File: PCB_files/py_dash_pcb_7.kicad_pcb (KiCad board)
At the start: 4 copper layers, 203.8 x 102.4 mm, 104 parts, among them J1 FFC2B28-40-G, J2 CANbus, J3 uUSB, Q1 DMG2307, Q2 DMG2307, Q3 DMG2307, SW1 SW_Push, SW2 SW_Push, SW3 SW_Push, SW4 SW_Push, SW5 SW_Push, SW6 SW_Push, SW7 nBoot, U1 CM4102008, U2 FSUSB42MUX, U3 AP64501SP-13, U4 TPD8S009DSMR, U5 TPD8S009DSMR, U6 TPD2EUSB30, U7 SN65HVD234, U8 MCP2515-xST, U9 BD33FC0FP, Y1 16Mhz

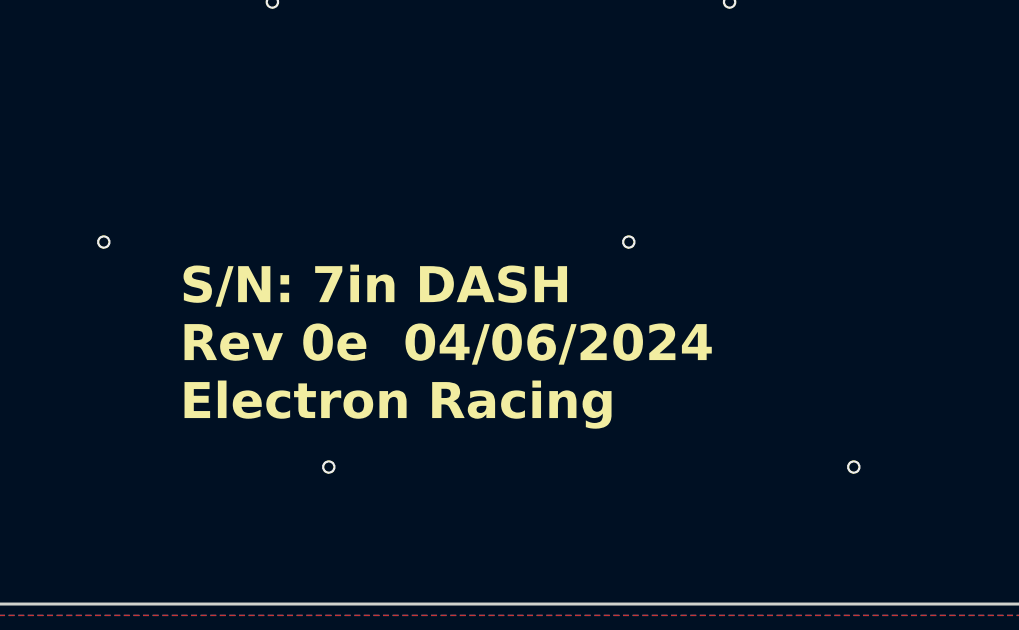
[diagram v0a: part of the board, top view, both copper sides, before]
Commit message: r1a upload
uploaded files for r1a; correct button numbering
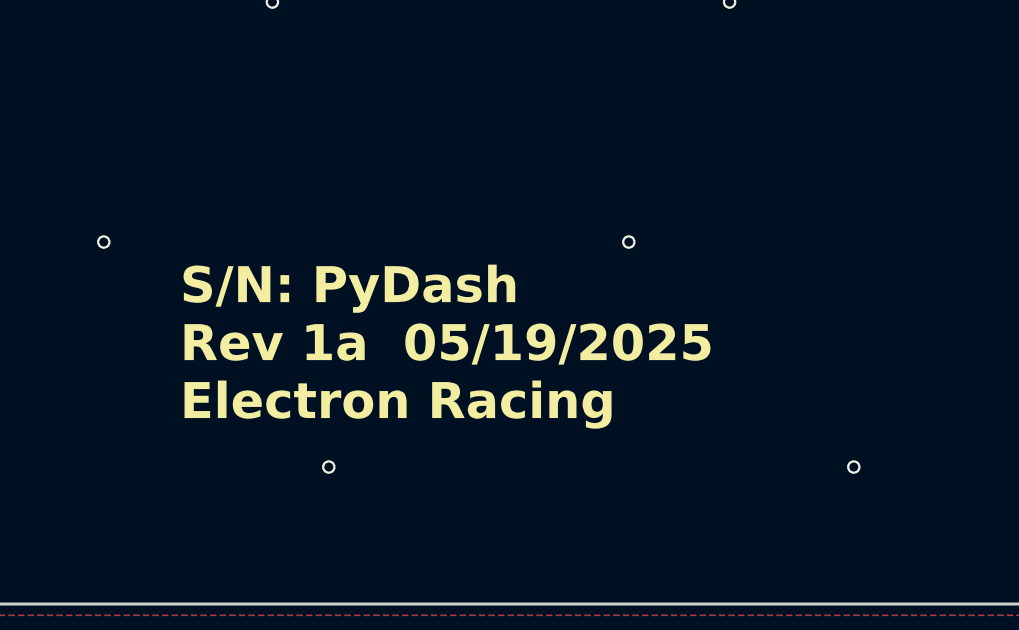
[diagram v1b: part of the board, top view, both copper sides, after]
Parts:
- R28, R29: value 2k2 -> 2k2 1%
- renumbered SW4 to SW1, SW5 to SW2, SW6 to SW3, SW1 to SW4, SW2 to SW5, SW3 to SW6
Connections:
- C26 pad 1: btn_L1 -> btn_R1
- C27 pad 1: btn_L2 -> btn_R2
- C28 pad 1: btn_L3 -> btn_R3
- C29 pad 1: btn_R1 -> btn_L1
- C30 pad 1: btn_R2 -> btn_L2
- C31 pad 1: btn_R3 -> btn_L3
- R15 pad 1: btn_L1 -> btn_R1
- R16 pad 1: btn_L2 -> btn_R2
- R17 pad 1: btn_L3 -> btn_R3
- R21 pad 1: btn_R1 -> btn_L1
- R22 pad 1: btn_R2 -> btn_L2
- R23 pad 1: btn_R3 -> btn_L3
- U1 pad 26: btn_R2 -> btn_L2
- U1 pad 30: btn_R3 -> btn_L3
- U1 pad 45: btn_R1 -> btn_L1
- U1 pad 48: btn_L3 -> btn_R3
- U1 pad 54: btn_L2 -> btn_R2
- U1 pad 58: btn_L1 -> btn_R1
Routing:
- net btn_R1: track 118.1 -> 95.6 mm, vias 0 -> 2
- net btn_L1: track 95.6 -> 118.1 mm, vias 2 -> 0
- net btn_R3: track 154.1 -> 138.1 mm
- net btn_L3: track 138.1 -> 154.1 mm
- net btn_R2: track 129.0 -> 114.8 mm
- net btn_L2: track 114.8 -> 129.0 mm
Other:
- board text added: "S/N: PyDash Rev 1a 05/19/2025 Electron Racing"
- board text removed: "S/N: 7in DASH Rev 0e 04/06/2024 Electron Racing"

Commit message: Rev2a initial upload
PCB files
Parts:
- removed C34: 0u1, Capacitor_SMD:C_0805_2012Metric
- removed J3: uUSB, user:GCT_USB3140-30-0170-1-C_REVE1
- removed R28, R29: 2k2 1%, Resistor_SMD:R_0805_2012Metric
- removed U2: FSUSB42MUX, Package_SO:MSOP-10_3x3mm_P0.5mm
- added C21: 0u1, Capacitor_SMD:C_0805_2012Metric, F.Cu at (215.2, 57.8)
- added C35: 10u, Capacitor_SMD:C_0805_2012Metric, F.Cu at (213.1, 57.8)
- added J5: Micro_SD_Card_Det1, Connector_Card:microSD_HC_Hirose_DM3AT-SF-PEJM5, F.Cu at (224.3, 53.6)
- added J8: USB_C_Receptacle_USB2.0_14P, Connector_USB:USB_C_Receptacle_GCT_USB4115-03-C, F.Cu at (198.2, 118.5)
- added U10: EMIF06-MSD02N16, user:EMIF06MSD02N16, F.Cu at (209.7, 60.9)
- moved U6 97.7 mm to (192.0, 115.9)
- moved C33 7.42 mm to (139.7, 48.4), turned to 180 degrees
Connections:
- J1 pad 7: tch_USBD- -> unconnected-(J1-Pad7)
- J1 pad 8: tch_USBD+ -> unconnected-(J1-Pad8)
- U1 pad 101: USB_OTG -> GND
- U1 pad 103: USBD- -> ext_USBD-
- U1 pad 105: USBD+ -> ext_USBD+
- U1 pad 24: unconnected-(U1A-GPIO26-Pad24) -> SD_DET
- U1 pad 57: unconnected-(U1A-SD_CLK-Pad57) -> SD_CLK
- U1 pad 61: unconnected-(U1A-SD_DAT3-Pad61) -> SD_DAT3
- U1 pad 62: unconnected-(U1A-SD_CMD-Pad62) -> SD_CMD
- U1 pad 63: unconnected-(U1A-SD_DAT0-Pad63) -> SD_DAT0
- U1 pad 67: unconnected-(U1A-SD_DAT1-Pad67) -> SD_DAT1
- U1 pad 69: unconnected-(U1A-SD_DAT2-Pad69) -> SD_DAT2
- U5 pad 4: tch_USBD- -> unconnected-(U5-D1+-Pad4)
- U5 pad 6: tch_USBD+ -> unconnected-(U5-D1--Pad6)
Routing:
- net SD_DET: track 0.00 -> 86.4 mm, vias 0 -> 2
- net SD_DAT2: track 0.00 -> 82.0 mm
- net SD_DAT1: track 0.00 -> 77.0 mm
- net SD_DAT0: track 0.00 -> 75.1 mm, vias 0 -> 2
- net SD_DAT3: track 0.00 -> 74.5 mm, vias 0 -> 2
- net SD_CLK: track 0.00 -> 70.8 mm, vias 0 -> 2
- net USB_OTG: track 68.6 -> 0.00 mm, vias 2 -> 0
- net SD_CMD: track 0.00 -> 68.1 mm, vias 0 -> 2
- net USBD-: track 57.7 -> 0.00 mm
- net USBD+: track 56.9 -> 0.00 mm
- net +3.3V: track 302.8 -> 350.5 mm, vias 22 -> 24
- net ext_USBD+: track 19.1 -> 58.3 mm, vias 0 -> 5
- net ext_USBD-: track 18.3 -> 55.3 mm, vias 0 -> 2
- net Net-(J5-DAT1): track 0.00 -> 31.3 mm
- net tch_USBD+: track 31.1 -> 0.00 mm
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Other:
- board text added: "S/N: PyDash Rev 2a 02/15/2025 LRC"
- board text added: "uSD"
- board text removed: "S/N: PyDash Rev 1a 05/19/2025 Electron Racing"

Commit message: push from desktop to align files
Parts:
- removed H7: MountingHole, MountingHole:MountingHole_3.2mm_M3_DIN965_Pad
- added H1: MountingHole_M2, MountingHole:MountingHole_3.2mm_M3_DIN965_Pad_TopOnly, F.Cu at (60.2, 57.4)
- added H10: Standoff_M2.5_5ET, user:Standoff_M2.5_5ET, F.Cu at (56.6, 108.7)
- added H11: Standoff_M2.5_5ET, user:Standoff_M2.5_5ET, F.Cu at (56.6, 141.6)
- added H12: Standoff_M2.5_5ET, user:Standoff_M2.5_5ET, F.Cu at (249.4, 50.2)
- added H13: Standoff_M2.5_5ET, user:Standoff_M2.5_5ET, F.Cu at (249.5, 83.1)
- added H14: Standoff_M2.5_5ET, user:Standoff_M2.5_5ET, F.Cu at (249.4, 108.6)
- added H15: Standoff_M2.5_5ET, user:Standoff_M2.5_5ET, F.Cu at (249.4, 141.6)
- added H16: Standoff_M2.5_5ET, user:Standoff_M2.5_5ET, F.Cu at (104.8, 50.1)
- added H17: Standoff_M2.5_5ET, user:Standoff_M2.5_5ET, F.Cu at (104.8, 141.5)
- added H18: Standoff_M2.5_5ET, user:Standoff_M2.5_5ET, F.Cu at (153.0, 50.2)
- added H19: Standoff_M2.5_5ET, user:Standoff_M2.5_5ET, F.Cu at (153.0, 141.3)
- added H20: Standoff_M2.5_5ET, user:Standoff_M2.5_5ET, F.Cu at (201.2, 50.2)
- added H21: Standoff_M2.5_5ET, user:Standoff_M2.5_5ET, F.Cu at (201.2, 141.3)
- added H22: Standoff_M2.5_5ET, user:Standoff_M2.5_5ET, F.Cu at (104.9, 95.8)
- added H23: Standoff_M2.5_5ET, user:Standoff_M2.5_5ET, F.Cu at (201.2, 95.8)
- added H3: MountingHole_M2, MountingHole:MountingHole_3.2mm_M3_DIN965_Pad_TopOnly, F.Cu at (60.2, 134.4)
- added H9: Standoff_M2.5_5ET, user:Standoff_M2.5_5ET, F.Cu at (56.6, 83.1)
- H5, H6: value MountingHole -> MountingHole_M2; footprint MountingHole:MountingHole_3.2mm_M3_DIN965_Pad -> MountingHole:MountingHole_3.2mm_M3_DIN965_Pad_TopOnly
- H8: value MountingHole -> Standoff_M2.5_5ET; footprint MountingHole:MountingHole_3.2mm_M3_DIN965_Pad -> user:Standoff_M2.5_5ET
- moved H5 207.0 mm to (245.8, 134.4)
- moved H8 91.3 mm to (56.6, 50.2)
- moved TP4 42.6 mm to (83.7, 138.8)
- moved J3 9.65 mm to (207.8, 119.7)
- moved U7 9.65 mm to (201.6, 117.1)
- moved H6 7.77 mm to (245.9, 57.3)
- moved C23 7.11 mm to (210.1, 52.8)
- moved C24 7.11 mm to (207.9, 52.8)
- moved SW1 6.42 mm to (116.3, 63.2), turned to 180 degrees
- moved J1 4.64 mm to (219.7, 53.3)
- moved D6 3.92 mm to (124.6, 138.9)
- moved R10 3.92 mm to (128.3, 138.9)
- moved TP3 3.92 mm to (131.7, 138.9)
- moved U4 3.92 mm to (206.6, 58.5), turned to -90 degrees
- moved D3 3.86 mm to (114.6, 131.6)
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- renumbered C33 to C1, C7 to C10, C9 to C11, C14 to C13, C16 to C14, C17 to C15, C18 to C16, C19 to C17, C20 to C18, C4 to C19, C32 to C2, C10 to C20, C3 to C21, C8 to C22, C21 to C23, C35 to C24, C22 to C25, C29 to C27, C27 to C28, C30 to C29, C11 to C3, C28 to C30, C23 to C32, C24 to C33, C25 to C34, C13 to C4, C1 to C5, C2 to C6, C15 to C7, C5 to C8, C6 to C9, D10 to D1, D7 to D2, D4 to D3, D5 to D4, D6 to D5, D1 to D6, D2 to D7, D3 to D8, D8 to D9, J5 to J1, J1 to J2, J8 to J3, J2 to J4, Q3 to Q2, Q2 to Q3, R27 to R1, R2 to R10, R3 to R11, R4 to R12, R18 to R13, R24 to R14, R21 to R16, R19 to R17, R25 to R18, R16 to R19, R9 to R2, R22 to R20, R14 to R21, R20 to R22, R26 to R23, R17 to R24, R23 to R25, R13 to R26, R11 to R3, R6 to R4, R10 to R5, R12 to R6, R5 to R8, R8 to R9, SW7 to SW1, SW4 to SW2, SW1 to SW3, SW5 to SW4, SW2 to SW5, SW3 to SW7, TP4 to TP1, TP1 to TP2, TP2 to TP3, TP3 to TP4, U3 to U2, U9 to U3, U10 to U4, U4 to U5, U5 to U6, U6 to U7, U7 to U9
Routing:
- net +3.3V: track 350.5 -> 364.2 mm, vias 24 -> 22
- net ext_USBD+: track 58.3 -> 68.3 mm
- net ext_USBD-: track 55.3 -> 65.4 mm
- net SD_DET: track 86.4 -> 78.9 mm, vias 2 -> 3
- net Net-(J1-DAT1): track 31.3 -> 24.0 mm
- net Net-(J1-DAT0): track 27.3 -> 21.6 mm
- net SD_DAT2: track 82.0 -> 76.3 mm
- net SD_CMD: track 68.1 -> 62.8 mm
- net Net-(J1-CLK): track 23.3 -> 18.5 mm
- net Net-(J1-CMD): track 19.1 -> 15.2 mm
- net btn_L1: track 120.3 -> 116.8 mm
- net Net-(J1-DAT3/CD): track 16.2 -> 13.3 mm
- net SD_DAT3: track 74.5 -> 72.0 mm, vias 2 -> 0
- net Net-(J1-DAT2): track 13.2 -> 11.5 mm
- net GND: track 4.85 -> 6.40 mm, vias 379 -> 400
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- added copper zone on F.Cu, net Net-(D4-K)
- removed copper zone on F.Cu, net Net-(D3-K)
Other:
- board size 203.8 x 102.4 mm -> 203.8 x 102.3 mm

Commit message: resolved tracker TODOs
Updated USBC placement to work with enclosure. Updated HDMI routes with chosen stackup to meet design requirements. Re-generated PCB fab files.
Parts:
- moved J3 10.9 mm to (218.7, 119.7)
- moved U7 10.9 mm to (212.5, 117.1)
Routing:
- net ext_USBD-: track 65.4 -> 76.3 mm
- net ext_USBD+: track 68.3 -> 79.3 mm
- net CK+: track 69.5 -> 74.6 mm
- net CK-: track 68.8 -> 73.8 mm
- net D0-: track 71.4 -> 75.4 mm
- net D0+: track 72.2 -> 76.1 mm
- net D2-: track 77.2 -> 76.3 mm
- net D2+: track 78.0 -> 77.0 mm
- net D1-: track 74.4 -> 73.8 mm
- net D1+: track 75.1 -> 74.6 mm
- added copper zone on F.Cu, net Net-(D3-K)
- removed copper zone on F.Cu, net Net-(D4-K)
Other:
- board text added: "PyDash - LRC Batch: B/N 03092025 Rev 2a 03/09/2025"
- board text added: "Stackup to be used: JLC04121H-3313 (or equivalent) - 1oz (0.035mm) outer layer - top/bot to inner layer separation 0.1mm Failure to use chosen or equivalent stackup may result in out of spec HDMI routing"
- board text removed: "S/N: PyDash Rev 2a 02/15/2025 LRC"

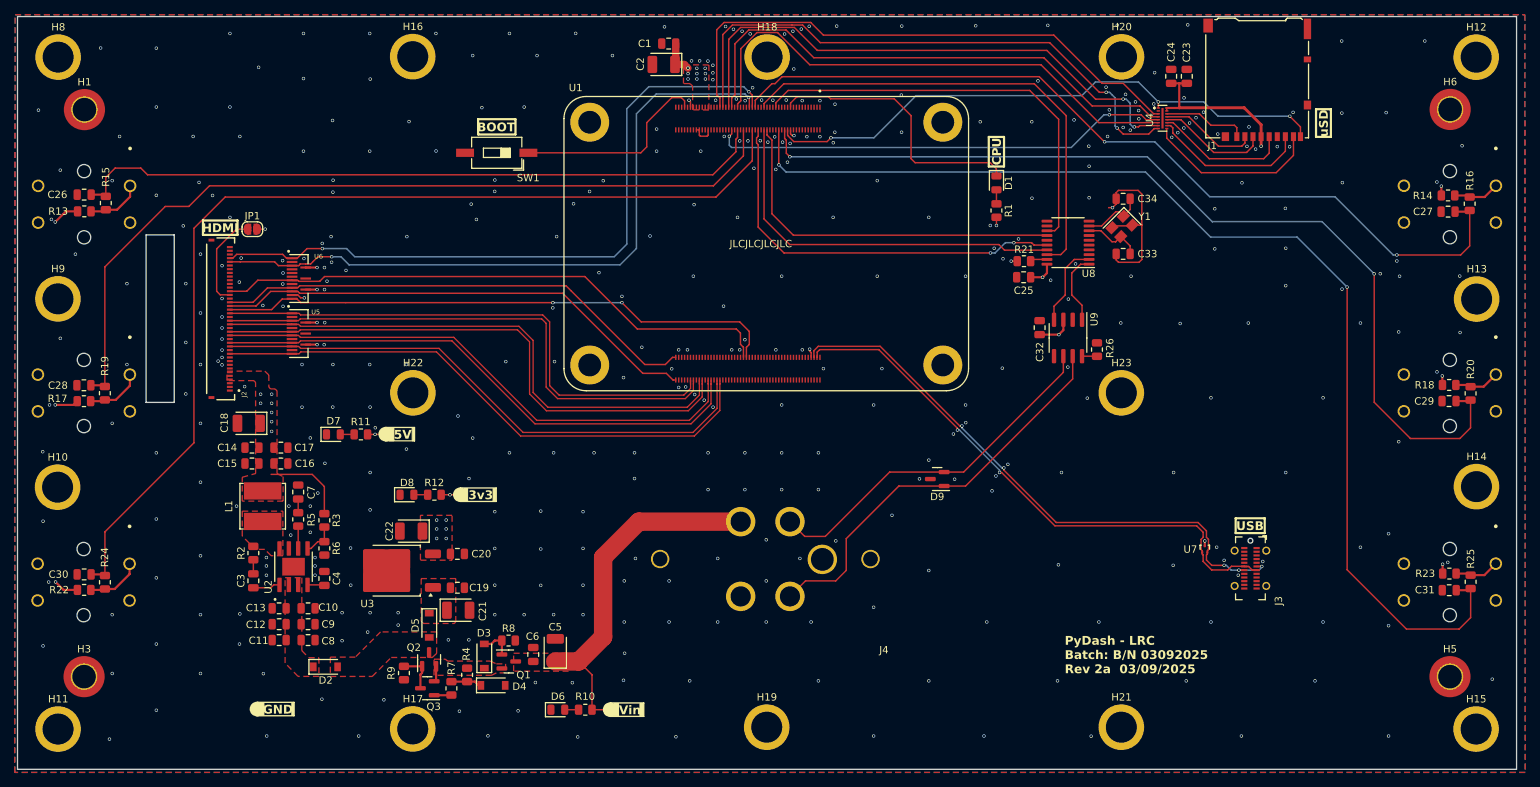
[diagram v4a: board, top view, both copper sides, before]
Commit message: final BOM and tweaking
Tweaked some dimensions after mechanical assembly. Generated BOM and reviewed against reseller inventory
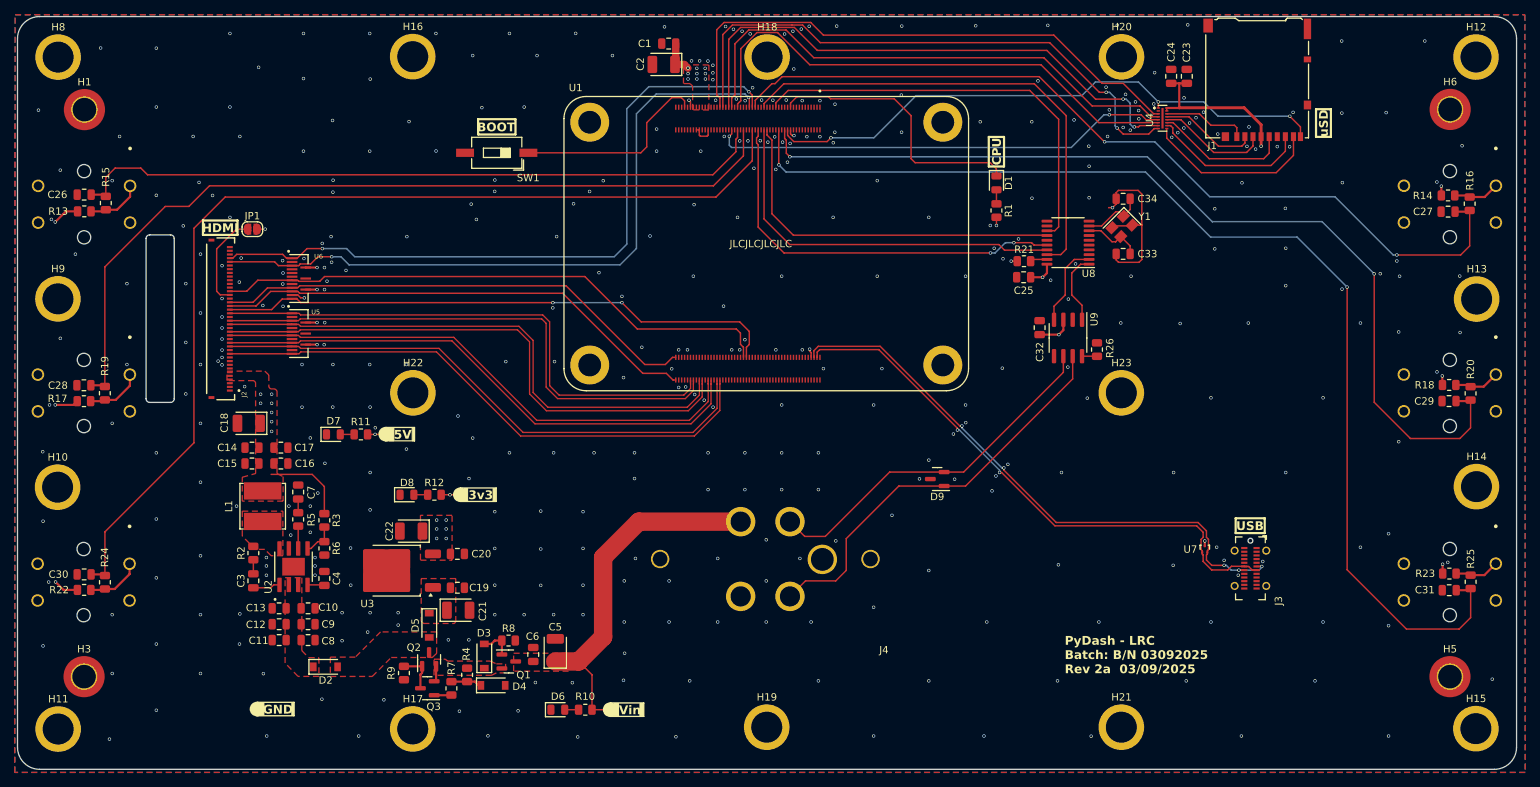
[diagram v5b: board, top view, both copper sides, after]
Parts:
- H10, H11, H12, H13, H14, H15, H16, H17, H18, H19, H20, H21, H22, H23, H8, H9: value Standoff_M2.5_5ET -> Standoff_M2.5_6ET; footprint user:Standoff_M2.5_5ET -> user:Standoff_M2.5_6ET
- moved H15 0.06 mm to (249.4, 141.5)
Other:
- outline, holes or cut-outs redrawn
